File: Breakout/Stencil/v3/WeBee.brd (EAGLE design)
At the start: 43.7 x 25.9 mm, 61 parts, among them U2 FT2232D, U3 LMR10510XMFE, U5 93LC46BT-I/OT

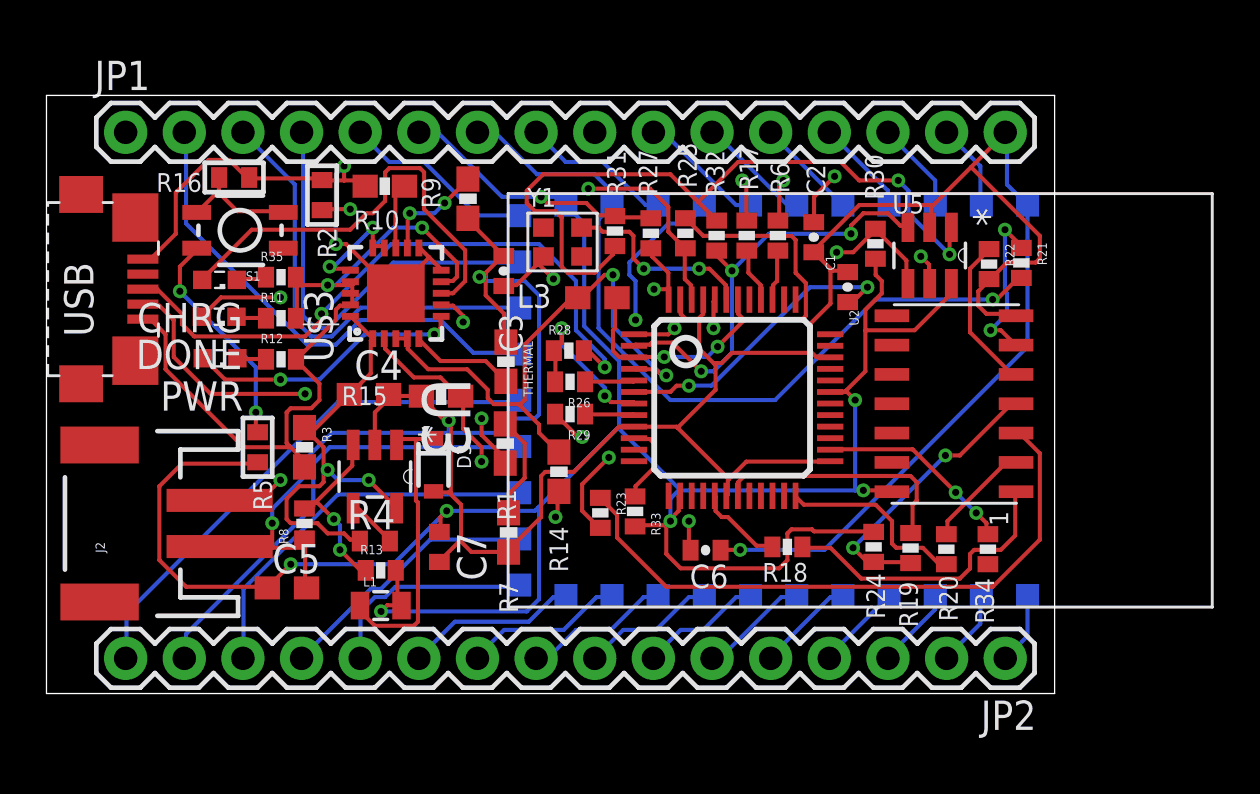
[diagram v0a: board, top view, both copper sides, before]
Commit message: Correct a mistake in lib
The lib was reversed
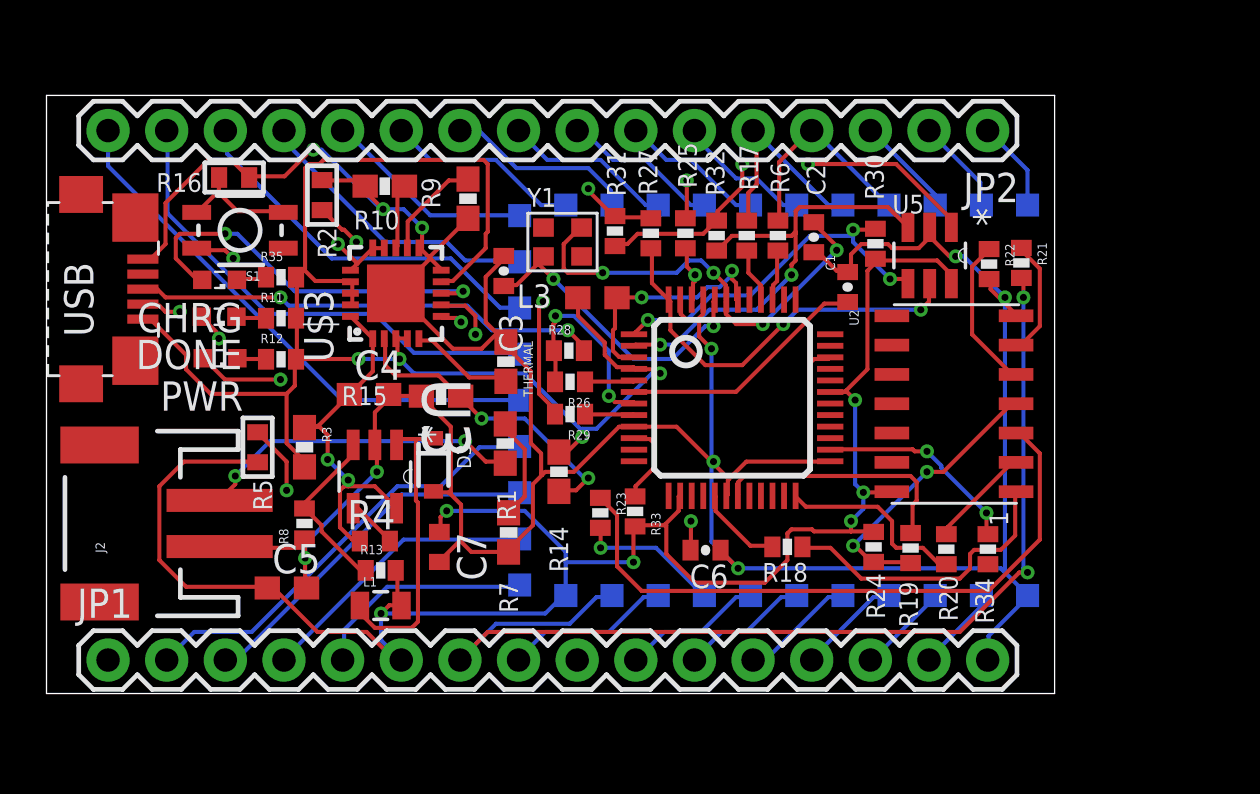
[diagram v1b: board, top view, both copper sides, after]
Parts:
- moved JP1 22.9 mm to (2.67, 1.45)
- moved JP2 22.9 mm to (40.8, 24.4)
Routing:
- net FTDI_TX: track 30.7 -> 9.38 mm, vias 1 -> 0
- net GND: track 173.2 -> 154.1 mm, vias 6 -> 10
- net FTDI_RX: track 27.2 -> 9.29 mm, vias 1 -> 0
- net VCC: track 115.3 -> 101.0 mm
- net N$54: track 32.0 -> 18.2 mm
- net N$51: track 27.6 -> 14.6 mm
- net RST: track 60.3 -> 73.2 mm, vias 3 -> 4
- net USB_D+: track 27.8 -> 20.3 mm
- net SOP2: track 32.8 -> 25.9 mm, vias 3 -> 2
- net N$29: track 18.8 -> 12.4 mm
- net +5V_USB_F: track 21.2 -> 16.8 mm, vias 2 -> 3
- net OUT: track 19.8 -> 15.5 mm
- net N$30: track 19.6 -> 15.8 mm
- net N$71: track 13.5 -> 16.9 mm
- net N$39: track 20.3 -> 17.6 mm
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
